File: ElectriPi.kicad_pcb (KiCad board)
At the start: 2 copper layers, 65 x 56 mm, 61 parts, among them IC2 TPS51397ARJER, J1 2444, J2 JST XH 01x02, J3 JST XH 01x02, J6 Raspberry_Pi_2_3, J8 JST XH 01x02, Q1 SiA471DJ, Q2 SiA430DJT, U1 LM74700

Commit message: Small cleanup
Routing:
- net +5V: track 26.6 -> 20.5 mm
- net Net-(D4-A): track 4.46 -> 3.95 mm
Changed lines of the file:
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@@
   (segment (start 139.75 91.25) (end 139.75 90.275) (width 0.5) (layer "F.Cu") (net 1))
   (segment (start 139.75 85.5) (end 139.75 86.24) (width 0.25) (layer "F.Cu") (net 1))
-  (segment (start 139.875 90.4) (end 139.75 90.275) (width 0.25) (layer "F.Cu") (net 1))
   (segment (start 146.75 83) (end 141 83) (width 0.25) (layer "F.Cu") (net 1))
   (segment (start 141.45 90.4) (end 139.875 90.4) (width 0.25) (layer "F.Cu") (net 1))
@@
   (via (at 135.05 64.85) (size 0.6) (drill 0.4) (layers "F.Cu" "B.Cu") (net 3))
   (via (at 135.45 68.2) (size 0.6) (drill 0.4) (layers "F.Cu" "B.Cu") (net 3))
-  (via (at 136.5 77.75) (size 0.6) (drill 0.4) (layers "F.Cu" "B.Cu") (net 3))
+  (via (at 143.5 78.25) (size 0.6) (drill 0.4) (layers "F.Cu" "B.Cu") (net 3))
   (via (at 135 76.5) (size 0.6) (drill 0.4) (layers "F.Cu" "B.Cu") (net 3))
   (segment (start 135 75) (end 135 73.5) (width 1) (layer "B.Cu") (net 3))
-  (segment (start 141.25 77.75) (end 136.5 77.75) (width 0.5) (layer "B.Cu") (net 3))
+  (segment (start 143.5 78.25) (end 143.5 85) (width 0.5) (layer "B.Cu") (net 3))
   (segment (start 135.45 68.2) (end 134 68.2) (width 1) (layer "B.Cu") (net 3))
-  (segment (start 143.5 85) (end 143.5 80) (width 0.5) (layer "B.Cu") (net 3))
   (segment (start 135.45 68.2) (end 135.05 67.8) (width 0.5) (layer "B.Cu") (net 3))
   (segment (start 135 75) (end 135 76.5) (width 1) (layer "B.Cu") (net 3))
   (segment (start 135.05 67.8) (end 135.05 64.85) (width 0.5) (layer "B.Cu") (net 3))
-  (segment (start 143.5 80) (end 141.25 77.75) (width 0.5) (layer "B.Cu") (net 3))
   (via (at 147.25 71.5) (size 0.6) (drill 0.4) (layers "F.Cu" "B.Cu") (free) (net 4))
   (via (at 141.5 95) (size 0.6) (drill 0.4) (layers "F.Cu" "B.Cu") (net 4))
@@
   (segment (start 140.75 95.75) (end 140 96.5) (width 1) (layer "B.Cu") (net 4))
   (segment (start 140.75 95.75) (end 141.5 95) (width 1) (layer "B.Cu") (net 4))
-  (segment (start 149.1 71.1125) (end 149.2 71.2125) (width 0.5) (layer "F.Cu") (net 5))
   (segment (start 149.1 70.01) (end 149.1 71.1125) (width 0.5) (layer "F.Cu") (net 5))
   (segment (start 149.5 77.8875) (end 149.2 77.5875) (width 0.5) (layer "F.Cu") (net 6))
   (segment (start 149.5 78.99) (end 149.5 77.8875) (width 0.5) (layer "F.Cu") (net 6))
   (segment (start 142 92.3) (end 142 93.73) (width 0.25) (layer "F.Cu") (net 7))
-  (segment (start 142 93.73) (end 141.98 93.75) (width 0.25) (layer "F.Cu") (net 7))
   (segment (start 135.05 66.1375) (end 134.3875 66.1375) (width 0.5) (layer "F.Cu") (net 8))
   (segment (start 133.25 65) (end 133.25 61.5) (width 0.5) (layer "F.Cu") (net 8))
@@
   (segment (start 142.52 103.75) (end 142.52 102.2175) (width 0.5) (layer "F.Cu") (net 43))
   (segment (start 141.1 101.75) (end 142.55 101.75) (width 0.25) (layer "F.Cu") (net 43))
-  (segment (start 142.5 103.77) (end 142.52 103.75) (width 0.5) (layer "F.Cu") (net 43))
-  (segment (start 142.52 102.2175) (end 142.55 102.1875) (width 0.5) (layer "F.Cu") (net 43))
-  (segment (start 142.55 101.75) (end 142.55 102.1875) (width 0.25) (layer "F.Cu") (net 43))
   (via (at 122.5 103) (size 0.6) (drill 0.4) (layers "F.Cu" "B.Cu") (net 44))
   (via (at 119.5 103) (size 0.6) (drill 0.4) (layers "F.Cu" "B.Cu") (net 44))
@@
   (segment (start 144.35 90.4) (end 145.59 90.4) (width 0.25) (layer "F.Cu") (net 46))
   (segment (start 145.59 90.4) (end 145.74 90.25) (width 0.25) (layer "F.Cu") (net 46))
-  (segment (start 144.75 87.99) (end 144.74 88) (width 0.25) (layer "F.Cu") (net 48))
   (segment (start 143.35 88.86967) (end 144.21967 88) (width 0.25) (layer "F.Cu") (net 48))
   (segment (start 144.21967 88) (end 144.74 88) (width 0.25) (layer "F.Cu") (net 48))
@@
   (segment (start 144.75 86.76) (end 144.75 87.99) (width 0.25) (layer "F.Cu") (net 48))
   (segment (start 142.5 86.01) (end 142.5 87.24) (width 0.25) (layer "F.Cu") (net 49))
-  (segment (start 142.45 87.29) (end 142.49 87.25) (width 0.25) (layer "F.Cu") (net 49))
   (segment (start 142.45 89.4) (end 142.45 87.29) (width 0.25) (layer "F.Cu") (net 49))
-  (segment (start 142.5 87.24) (end 142.49 87.25) (width 0.25) (layer "F.Cu") (net 49))
   (segment (start 141.25 87.26) (end 139.75 87.26) (width 0.25) (layer "F.Cu") (net 50))
   (segment (start 142 89.4) (end 142 88.01) (width 0.25) (layer "F.Cu") (net 50))
@@
         (xy 149.5 69.25)
         (xy 144.75 69.25)
-        (xy 144.75 76.5)
-        (xy 142.5 78.75)
+        (xy 144.75 78)
+        (xy 144 78.75)
         (xy 137 78.75)
         (xy 137 89)

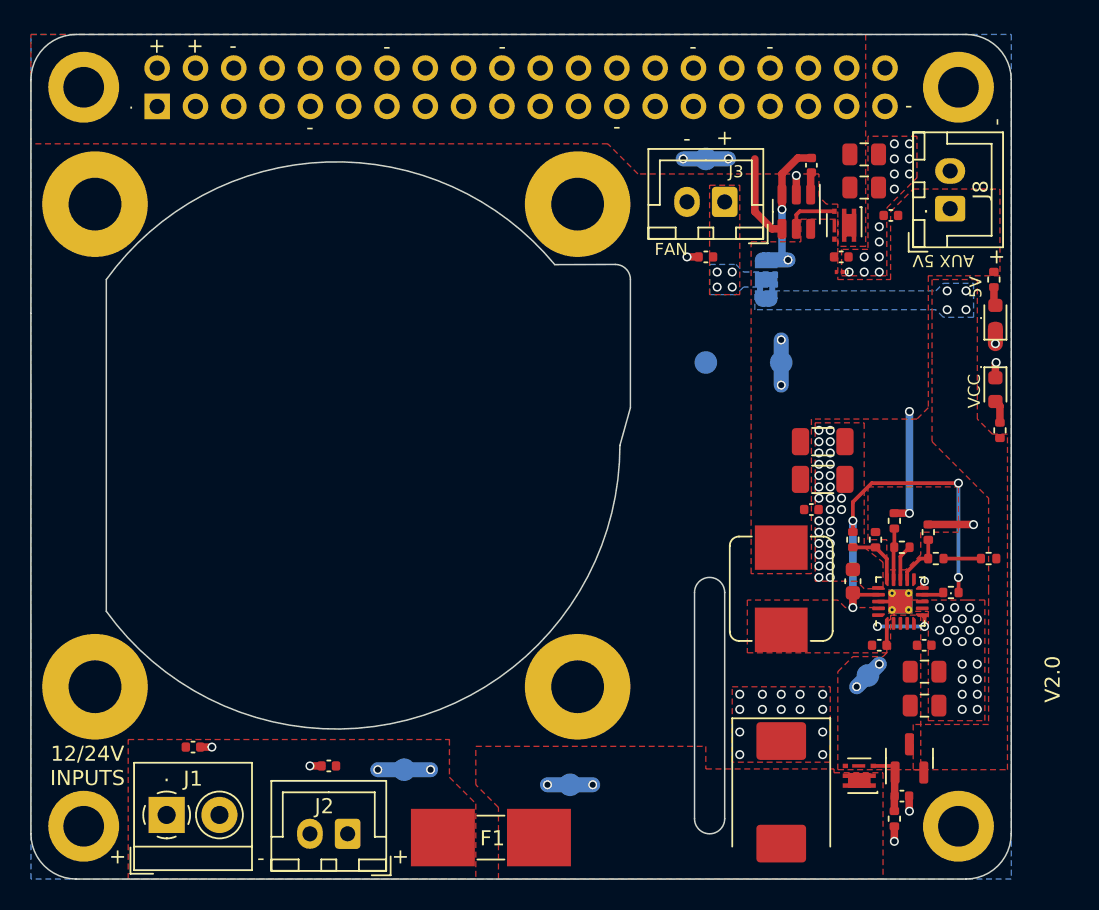
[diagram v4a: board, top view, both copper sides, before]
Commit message: changes to copper pours to satisfy DRC
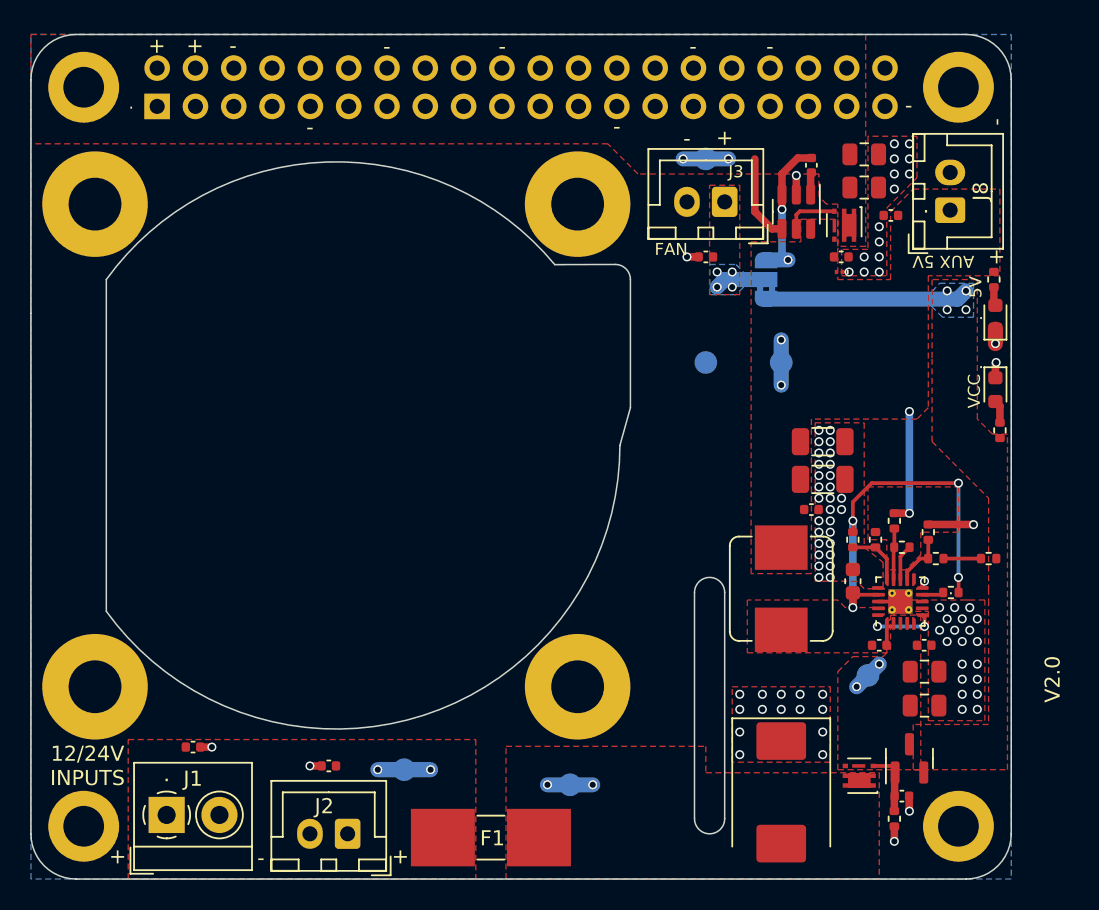
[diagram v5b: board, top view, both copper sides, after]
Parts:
- moved J8 0.10 mm to (146.2, 64.9)
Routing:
- net Vin: track 2.12 -> 15.6 mm
- net Net-(J3-Pin_1): track 0.00 -> 3.46 mm
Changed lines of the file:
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@@
   (net 52 "Net-(R1-Pad1)")
   (footprint "Connector_JST:JST_XH_B2B-XH-A_1x02_P2.50mm_Vertical" (layer "F.Cu")
-    (at 146.2 64.8 90)
+    (at 146.2 64.9 90)
     (descr "JST XH series connector, B2B-XH-A (http://www.jst-mfg.com/product/pdf/eng/eXH.pdf), generated with kicad-footprint-generator")
     (tags "connector JST XH vertical")
@@
     (effects (font (size 0.8 0.8) (thickness 0.15)))
   )
-  (gr_text "AUX 5V" (at 145.75 68.25 180) (layer "F.SilkS")
+  (gr_text "AUX 5V" (at 145.75 68.3 180) (layer "F.SilkS")
     (effects (font (size 0.8 0.8) (thickness 0.125)))
   )
@@
   (via (at 147.25 70.25) (size 0.6) (drill 0.4) (layers "F.Cu" "B.Cu") (free) (net 4))
   (segment (start 140.75 95.75) (end 140 96.5) (width 1) (layer "B.Cu") (net 4))
+  (segment (start 146.7 70.8) (end 134 70.8) (width 1) (layer "B.Cu") (net 4))
   (segment (start 140.75 95.75) (end 141.5 95) (width 1) (layer "B.Cu") (net 4))
+  (segment (start 147.25 70.25) (end 146.7 70.8) (width 1) (layer "B.Cu") (net 4))
   (segment (start 149.1 70.01) (end 149.1 71.1125) (width 0.5) (layer "F.Cu") (net 5))
   (segment (start 149.5 77.8875) (end 149.2 77.5875) (width 0.5) (layer "F.Cu") (net 6))
@@
   (via (at 131.75 70) (size 0.6) (drill 0.4) (layers "F.Cu" "B.Cu") (free) (net 42))
   (via (at 130.75 69) (size 0.6) (drill 0.4) (layers "F.Cu" "B.Cu") (free) (net 42))
+  (segment (start 134 69.5) (end 131.25 69.5) (width 1) (layer "B.Cu") (net 42))
+  (segment (start 131.25 69.5) (end 130.75 70) (width 1) (layer "B.Cu") (net 42))
   (segment (start 142.5 104.74) (end 142.5 103.77) (width 0.5) (layer "F.Cu") (net 43))
   (segment (start 142.52 103.75) (end 142.52 102.2175) (width 0.5) (layer "F.Cu") (net 43))
@@
         (xy 91.7 109.25)
         (xy 91.7 100)
-        (xy 113 100)
-        (xy 113 102.5)
-        (xy 114.75 104.25)
+        (xy 114.75 100)
       )
     )
@@
     (polygon
       (pts
-        (xy 141.75 109.25)
-        (xy 116.25 109.25)
-        (xy 116.25 104.5)
-        (xy 114.75 103)
-        (xy 114.75 100.45)
+        (xy 141.5 109.25)
+        (xy 116.75 109.25)
+        (xy 116.75 100.45)
         (xy 130 100.45)
-        (xy 130 101.95)
-        (xy 138.5 101.95)
-        (xy 138.5 102.2)
-        (xy 141.75 102.2)
+        (xy 130 102.2)
+        (xy 141.5 102.2)
       )
     )
@@
         (xy 132 68.5)
         (xy 132.5 69)
-        (xy 134.75 69)
-        (xy 134.75 70)
+        (xy 132.5 69)
+        (xy 132.5 70)
         (xy 132.5 70)
         (xy 132 70.5)
@@
     (polygon
       (pts
-        (xy 133.25 70.25)
-        (xy 145.25 70.25)
-        (xy 145.75 69.75)
+        (xy 145 70.3)
+        (xy 145.5 69.75)
         (xy 147.75 69.75)
         (xy 147.75 72)
-        (xy 145.75 72)
-        (xy 145.25 71.5)
-        (xy 133.25 71.5)
+        (xy 145.7 72)
+        (xy 145 71.3)
       )
     )

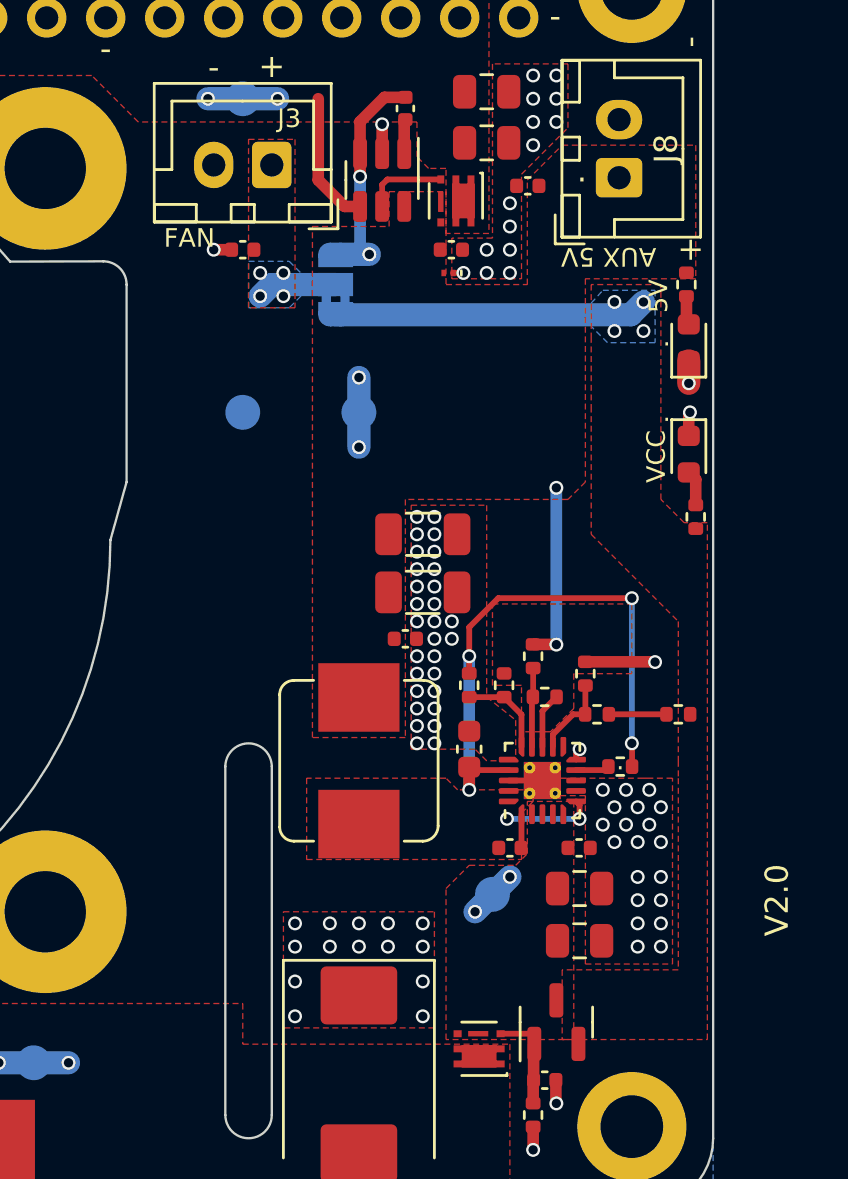
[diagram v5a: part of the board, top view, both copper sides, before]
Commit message: Changed to higher current inductor, which had larger footprint
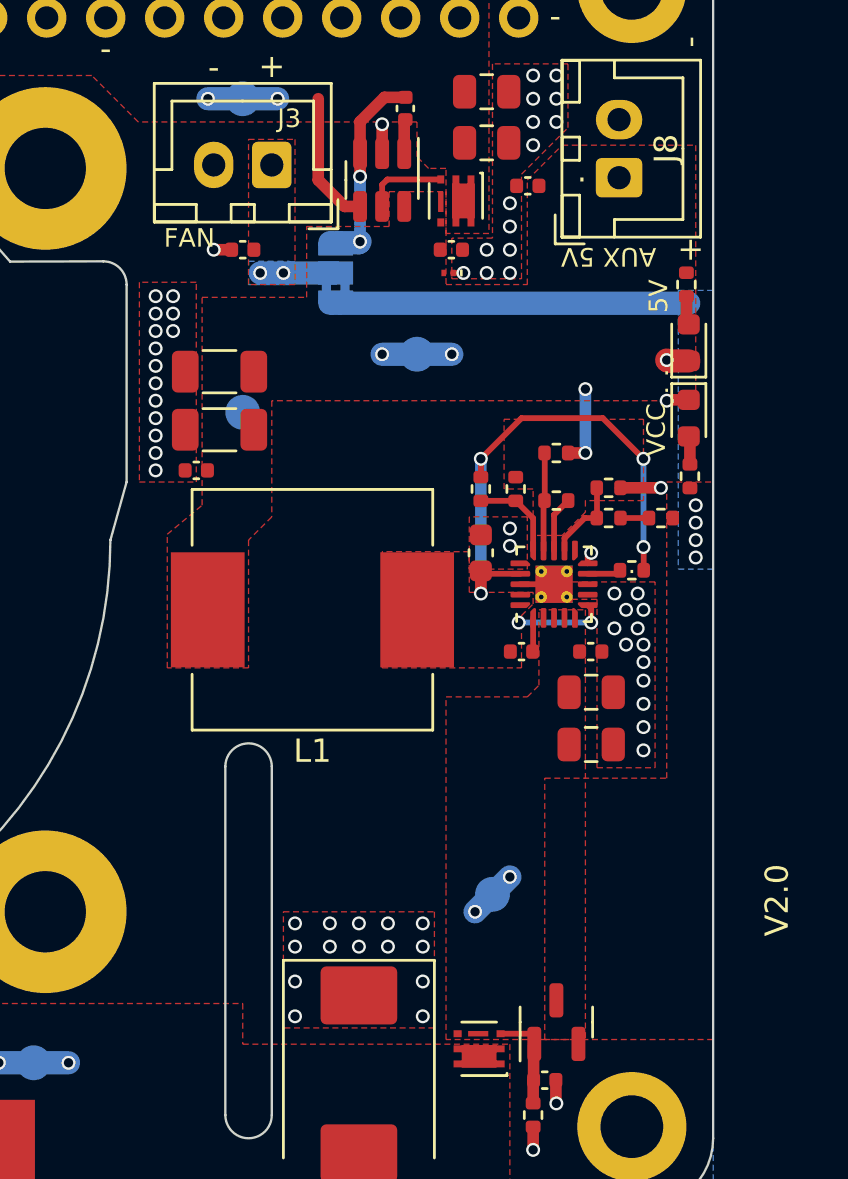
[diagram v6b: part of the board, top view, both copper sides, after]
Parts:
- L1: footprint Inductor_SMD:L_Bourns_SRP7028A_7.3x6.6mm -> Inductor_SMD:L_Vishay_IHLP-4040
- moved C5 12.9 mm to (129.0, 73.2), turned to 180 degrees
- moved C7 11.6 mm to (128.0, 77.5), turned to 180 degrees
- moved C4 9.84 mm to (129.0, 75.8), turned to 180 degrees
- moved R13 8.81 mm to (143.5, 76.8), turned to 180 degrees
- moved R1 8.48 mm to (148.0, 79.5)
- moved C1 8.46 mm to (145.0, 89.3)
- moved C2 8.46 mm to (145.0, 87.0)
- moved C3 8.46 mm to (140.2, 81.0)
- moved C6 8.46 mm to (145.0, 85.3)
- moved C8 8.46 mm to (142.0, 85.3)
- moved R12 8.46 mm to (146.8, 81.8)
- moved R14 8.46 mm to (143.5, 78.8)
- moved R4 8.46 mm to (140.2, 78.3)
- moved R5 8.46 mm to (141.8, 78.3)
- moved R7 8.46 mm to (145.8, 79.5)
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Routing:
- net +5V: track 20.5 -> 15.1 mm
- net VCC: track 25.1 -> 22.4 mm
- net Vin: track 15.6 -> 17.3 mm
- net GND: track 15.4 -> 14.1 mm, vias 87 -> 67
- net Net-(R1-Pad1): track 2.48 -> 1.23 mm
- net FB: track 3.34 -> 4.15 mm
- net Net-(J3-Pin_1): track 3.46 -> 3.25 mm, vias 4 -> 2

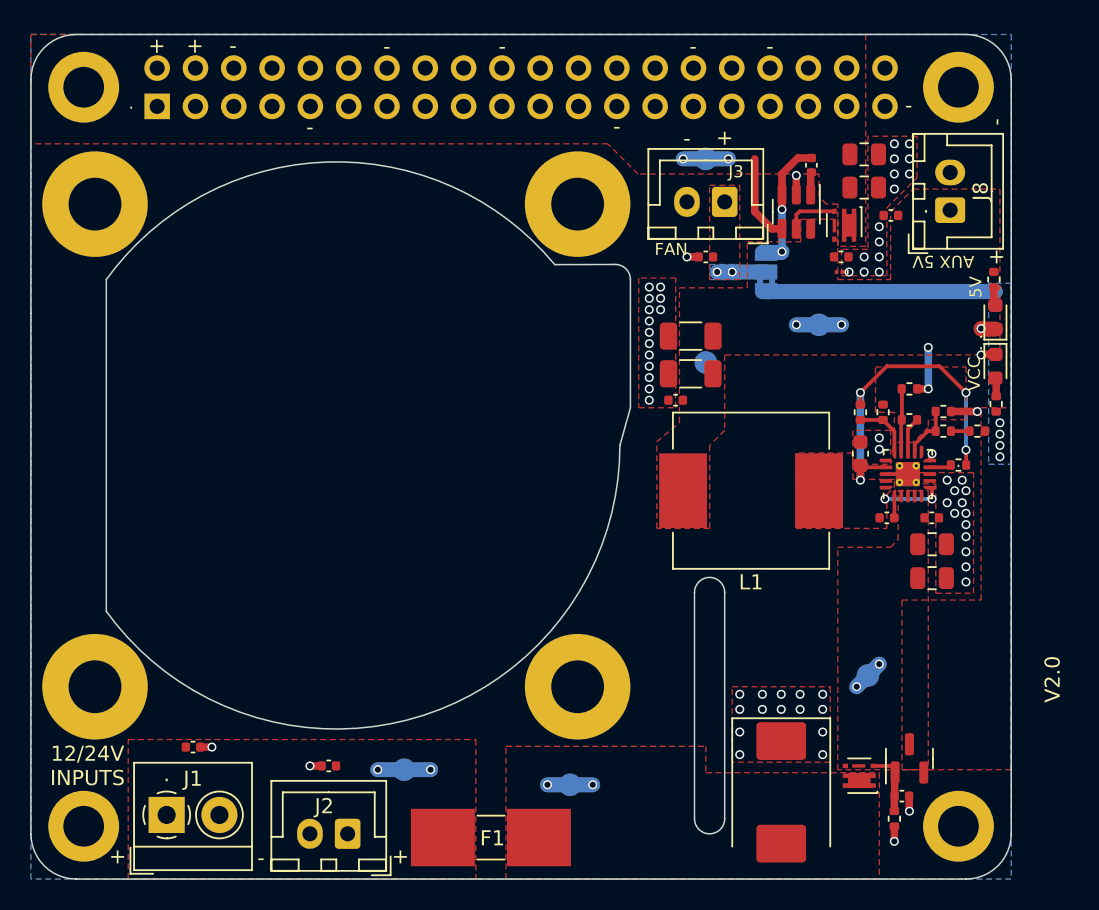
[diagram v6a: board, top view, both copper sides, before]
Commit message: Add bulk capacitance and update cap size
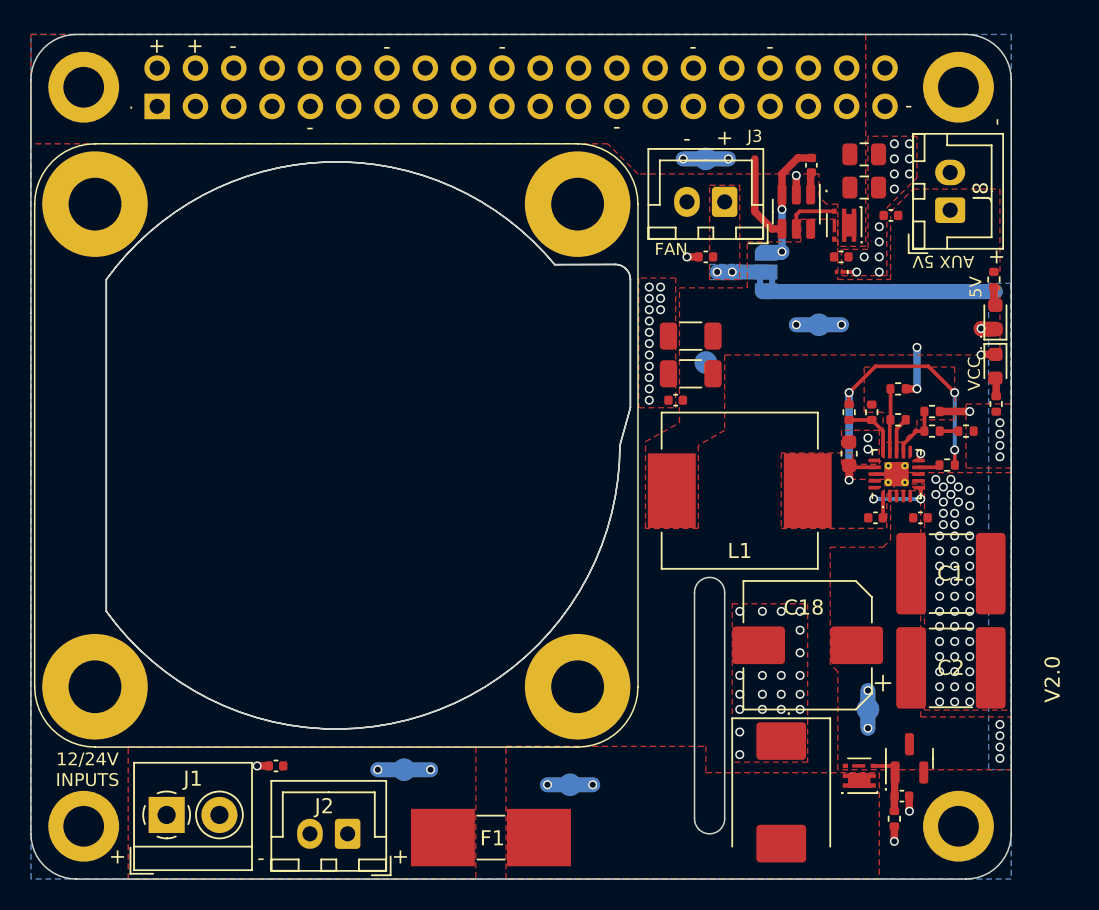
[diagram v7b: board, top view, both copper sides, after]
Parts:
- removed C12: 0.1uF, Capacitor_SMD:C_0402_1005Metric
- removed H5, H6, H7, H8: MountingHole, MountingHole:MountingHole_3.5mm_Pad
- added C18: 100uF, Capacitor_SMD:CP_Elec_8x10, F.Cu at (136.8, 93.8)
- added U2: COOLING, FAN:4040, F.Cu at (105.5, 80.5)
- C1, C2: footprint Capacitor_SMD:C_0805_2012Metric -> Capacitor_SMD:C_2220_5650Metric_Pad1.97x5.40mm_HandSolder
- moved G*** 9.52 mm to (141.2, 75.0)
- moved C2 8.29 mm to (146.2, 95.2)
- moved G*** 4.76 mm to (134.0, 78.2)
- moved C13 3.50 mm to (101.5, 101.8)
- moved TP4 2.25 mm to (140.8, 98.0)
- moved C1 1.29 mm to (146.2, 89.0)
- moved C3 0.75 mm to (139.5, 81.0)
- moved C6 0.75 mm to (144.2, 85.3)
- moved C8 0.75 mm to (141.2, 85.3)
- moved IC2 0.75 mm to (142.7, 82.4)
- moved L1 0.75 mm to (132.2, 83.5)
- moved R1 0.75 mm to (147.2, 79.5)
- moved R11 0.75 mm to (145.0, 78.2)
- moved R12 0.75 mm to (146.0, 81.8)
- moved R13 0.75 mm to (142.8, 76.8)
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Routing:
- net Vin: track 17.3 -> 17.7 mm, vias 6 -> 10
- net GND: track 14.1 -> 14.0 mm, vias 67 -> 109
